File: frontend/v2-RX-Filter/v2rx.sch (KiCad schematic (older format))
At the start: 130 parts, among them P1 CONN_02X07, P2 CONN_01X02, P5 CONN_01X02, U1 4504, U10 PE4259-53, U11 PE4259-53, U12 PE4259-53, U13 PE4259-53, U14 PE4259-53, U15 PE4259-53, U16 PE4259-53, U2 PE4259-53, U3 PE4259-53, U4 PE4259-53, U5 PE4259-53, U6 PE4259-53, U7 PE4259-53, U8 PE4259-53, U9 4504

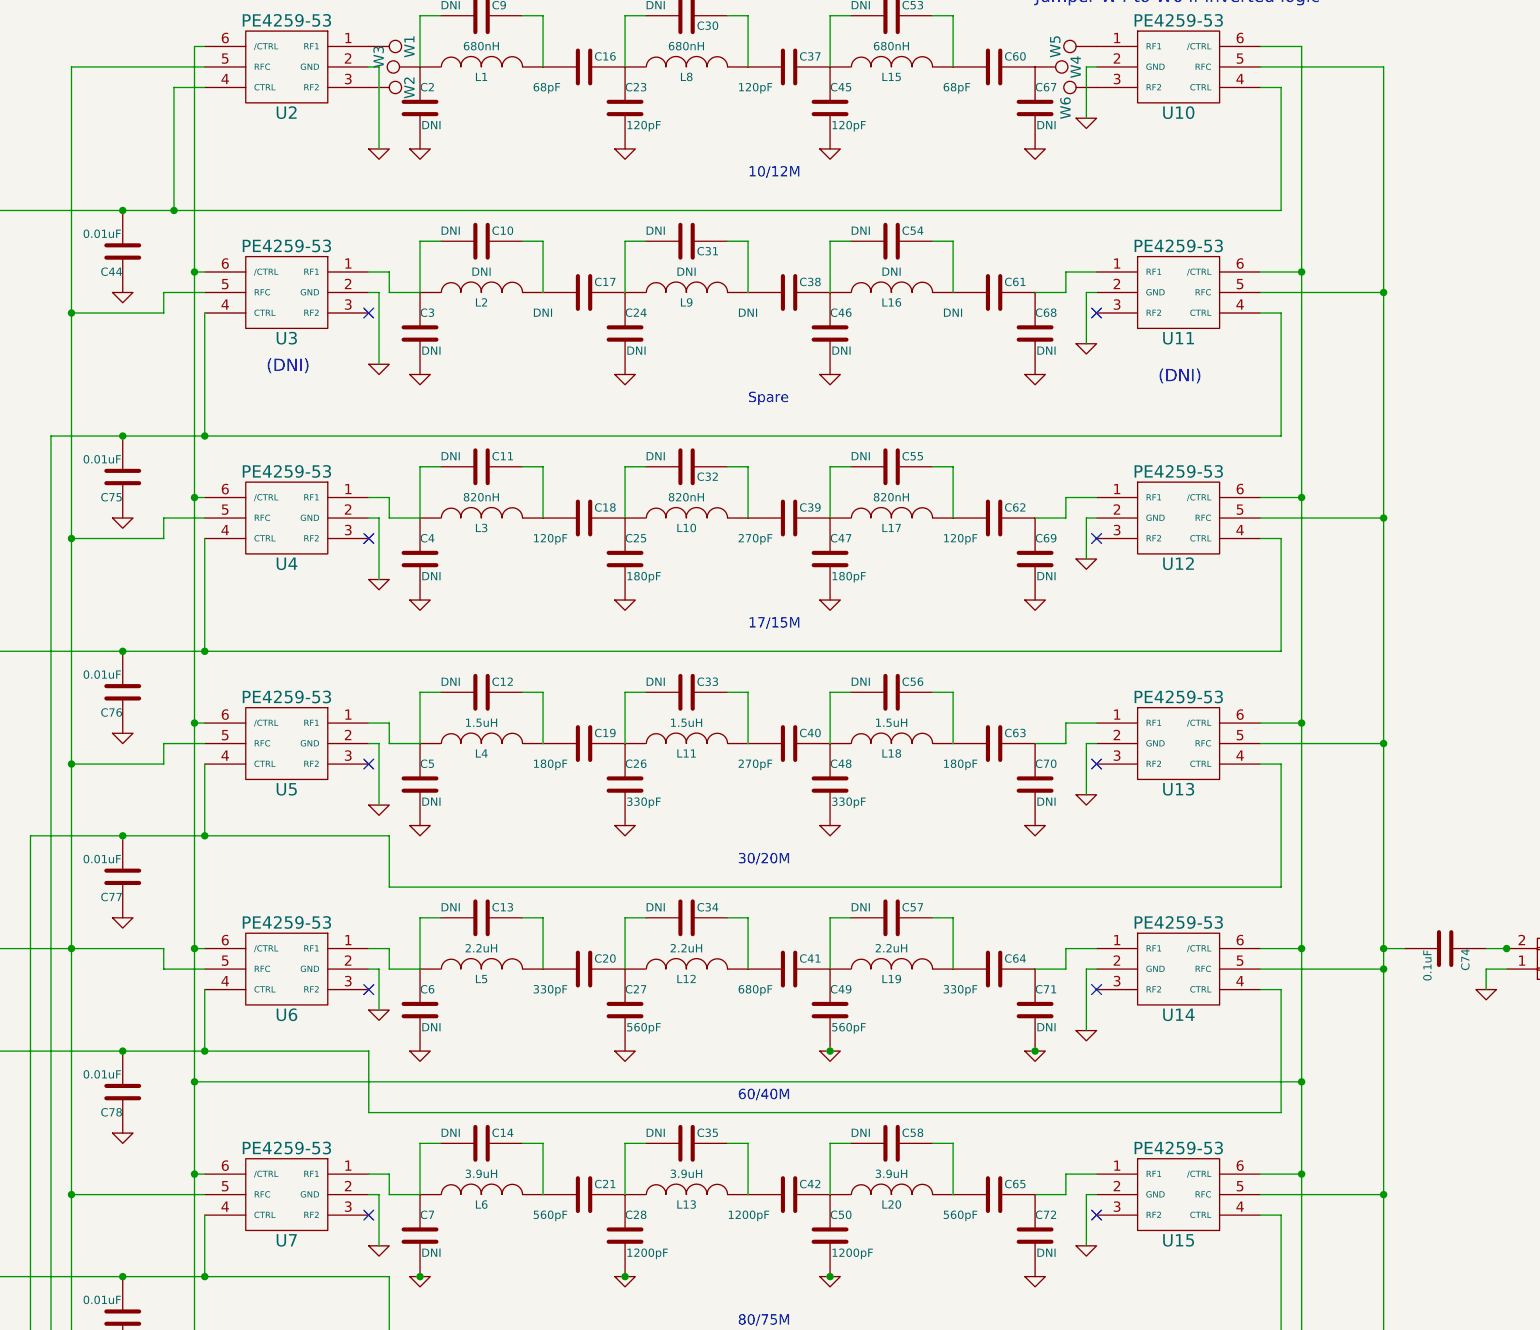
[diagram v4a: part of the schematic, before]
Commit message: Added additional bypass caps
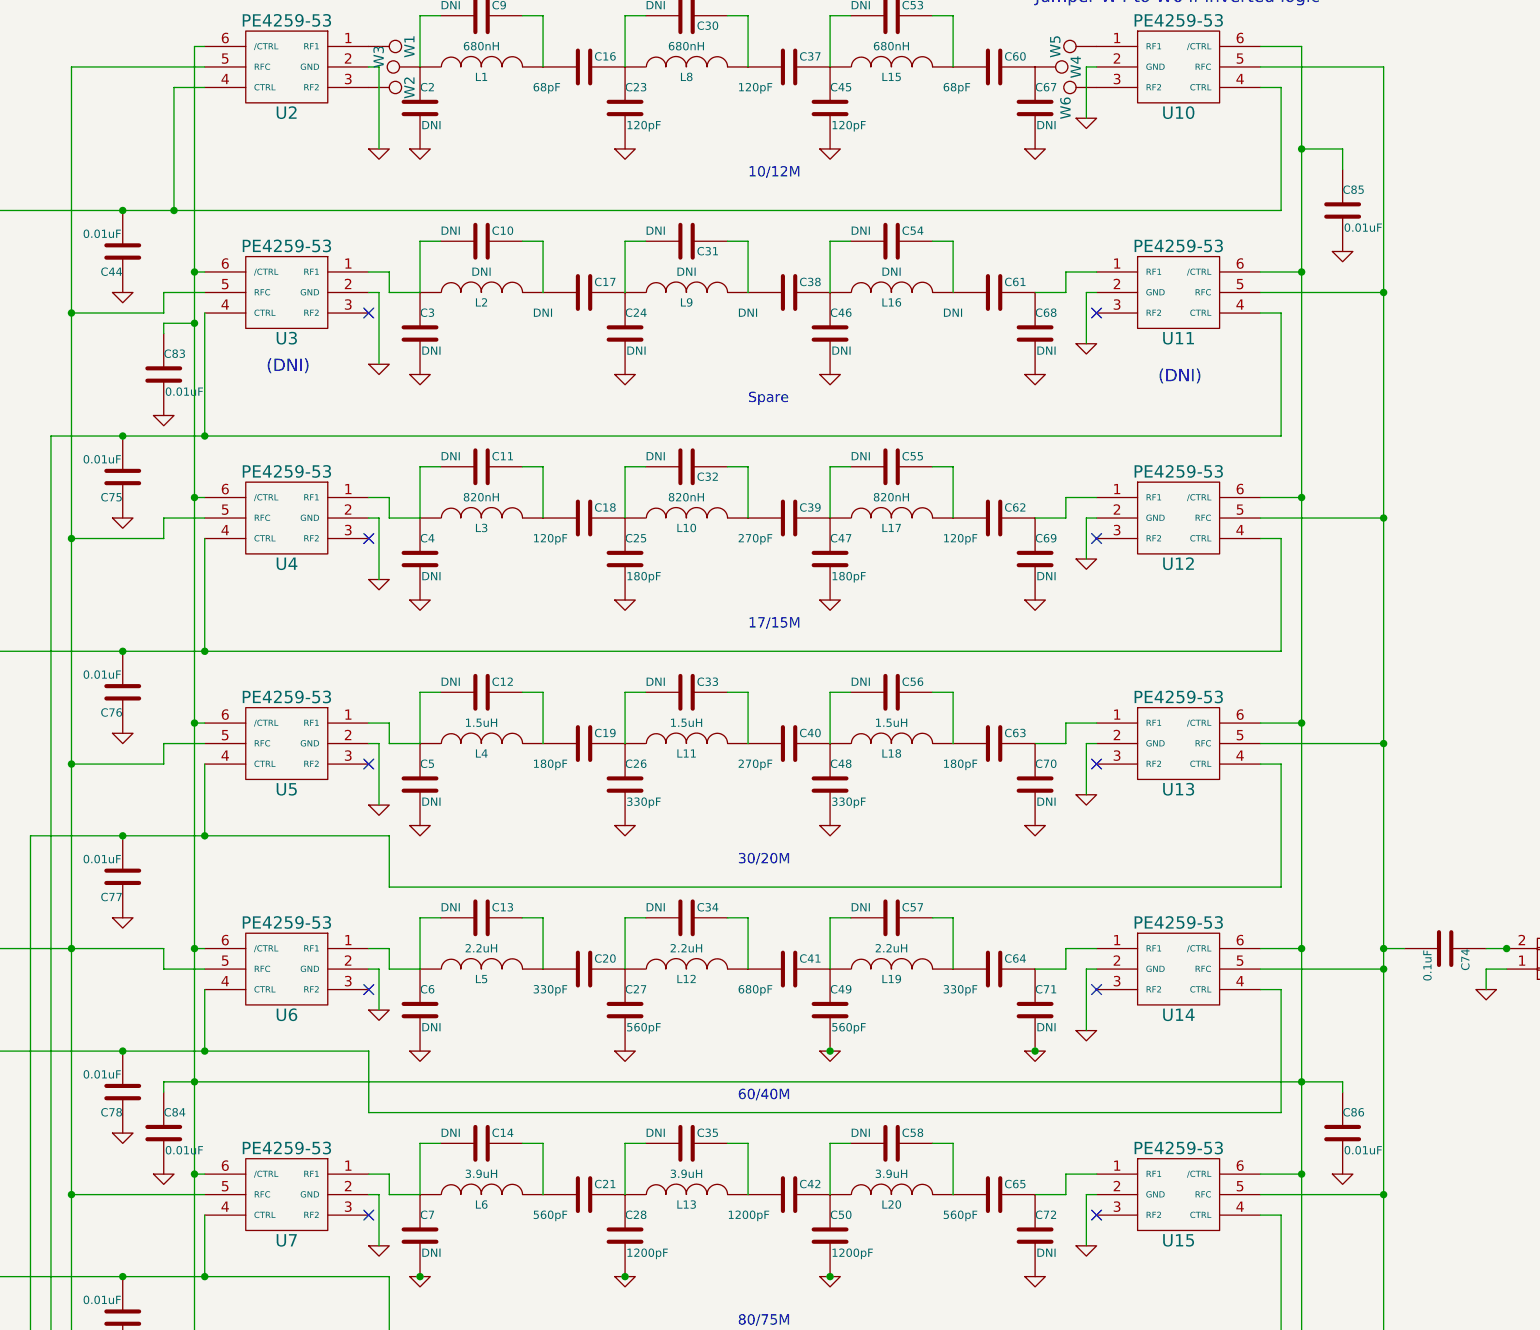
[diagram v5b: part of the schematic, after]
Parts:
- added C83, C84, C85, C86: 0.01uF, HERMESLITE:C_0805, symbol C-RESCUE-v2rx
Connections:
- net GND: now also C83.2, C84.2, C85.2, C86.2
- net at C81.2, FB2.2, U1.16 (VDD)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: now also C83.1, C84.1, C85.1, C86.1
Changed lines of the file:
@@
 	2850 5800 4750 5800
 Wire Wire Line
-	3900 5950 9300 5950
+	3750 5950 9500 5950
 Wire Wire Line
 	7000 4300 7000 4050
@@
 Text Notes 3900 650  0    60   ~ 0
 Jumper W3 to W1 if normal logic\nJumper W3 to W2 if inverted logic
+$Comp
+L C-RESCUE-v2rx C85
+U 1 1 56E74F71
+P 9500 1700
+F 0 "C85" H 9500 1800 40  0000 L CNN
+F 1 "0.01uF" H 9506 1615 40  0000 L CNN
+F 2 "HERMESLITE:C_0805" H 9538 1550 30  0001 C CNN
+F 3 "" H 9500 1700 60  0000 C CNN
+	1    9500 1700
+	1    0    0    -1
+$EndComp
+$Comp
+L GND-RESCUE-v2rx #PWR058
+U 1 1 56E7518A
+P 9500 1900
+F 0 "#PWR058" H 9500 1900 30  0001 C CNN
+F 1 "GND" H 9500 1830 30  0001 C CNN
+F 2 "" H 9500 1900 50  0000 C CNN
+F 3 "" H 9500 1900 50  0000 C CNN
+	1    9500 1900
+	1    0    0    -1
+$EndComp
+Wire Wire Line
+	9500 1500 9500 1400
+Wire Wire Line
+	9500 1400 9300 1400
+Connection ~ 9300 1400
+$Comp
+L C-RESCUE-v2rx C86
+U 1 1 56E7562B
+P 9500 6200
+F 0 "C86" H 9500 6300 40  0000 L CNN
+F 1 "0.01uF" H 9506 6115 40  0000 L CNN
+F 2 "HERMESLITE:C_0805" H 9538 6050 30  0001 C CNN
+F 3 "" H 9500 6200 60  0000 C CNN
+	1    9500 6200
+	1    0    0    -1
+$EndComp
+$Comp
+L GND-RESCUE-v2rx #PWR059
+U 1 1 56E765E7
+P 9500 6400
+F 0 "#PWR059" H 9500 6400 30  0001 C CNN
+F 1 "GND" H 9500 6330 30  0001 C CNN
+F 2 "" H 9500 6400 50  0000 C CNN
+F 3 "" H 9500 6400 50  0000 C CNN
+	1    9500 6400
+	1    0    0    -1
+$EndComp
+Wire Wire Line
+	9500 5950 9500 6000
+$Comp
+L C-RESCUE-v2rx C84
+U 1 1 56E76983
+P 3750 6200
+F 0 "C84" H 3750 6300 40  0000 L CNN
+F 1 "0.01uF" H 3756 6115 40  0000 L CNN
+F 2 "HERMESLITE:C_0805" H 3788 6050 30  0001 C CNN
+F 3 "" H 3750 6200 60  0000 C CNN
+	1    3750 6200
+	1    0    0    -1
+$EndComp
+$Comp
+L GND-RESCUE-v2rx #PWR060
+U 1 1 56E77C30
+P 3750 6400
+F 0 "#PWR060" H 3750 6400 30  0001 C CNN
+F 1 "GND" H 3750 6330 30  0001 C CNN
+F 2 "" H 3750 6400 50  0000 C CNN
+F 3 "" H 3750 6400 50  0000 C CNN
+	1    3750 6400
+	1    0    0    -1
+$EndComp
+Wire Wire Line
+	3750 6000 3750 5950
+$Comp
+L C-RESCUE-v2rx C83
+U 1 1 56E77FD1
+P 3750 2500
+F 0 "C83" H 3750 2600 40  0000 L CNN
+F 1 "0.01uF" H 3756 2415 40  0000 L CNN
+F 2 "HERMESLITE:C_0805" H 3788 2350 30  0001 C CNN
+F 3 "" H 3750 2500 60  0000 C CNN
+	1    3750 2500
+	1    0    0    -1
+$EndComp
+$Comp
+L GND-RESCUE-v2rx #PWR061
+U 1 1 56E797EF
+P 3750 2700
+F 0 "#PWR061" H 3750 2700 30  0001 C CNN
+F 1 "GND" H 3750 2630 30  0001 C CNN
+F 2 "" H 3750 2700 50  0000 C CNN
+F 3 "" H 3750 2700 50  0000 C CNN
+	1    3750 2700
+	1    0    0    -1
+$EndComp
+Wire Wire Line
+	3750 2300 3750 2250
+Wire Wire Line
+	3750 2250 3900 2250
+Connection ~ 3900 2250
 $EndSCHEMATC
